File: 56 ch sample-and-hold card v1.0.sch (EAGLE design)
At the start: 140 parts, among them IC1 74HCT4051D, IC10 TL074JT, IC11 74HCT4051D, IC12 TL074JT, IC13 TL074JT, IC14 74HCT4051D, IC15 TL074JT, IC16 TL074JT, IC17 74HCT4051D, IC18 TL074JT, IC19 TL074JT, IC2 DAC8586D, IC20 74HCT4051D, IC21 TL074JT, IC22 TL074JT, IC26 74HCT4051D, IC27 TL074JT, IC28 TL074JT, IC3 TL074JT, IC5 78L05F, IC6 TL074JT, IC7 74HCT4051D, IC8 TL074JT, IC9 TL074JT, X2 FEMALE, X3 FEMALE, X4 DNM, X5 DNM, X7 FEMALE, X8 FEMALE, X9 DNM

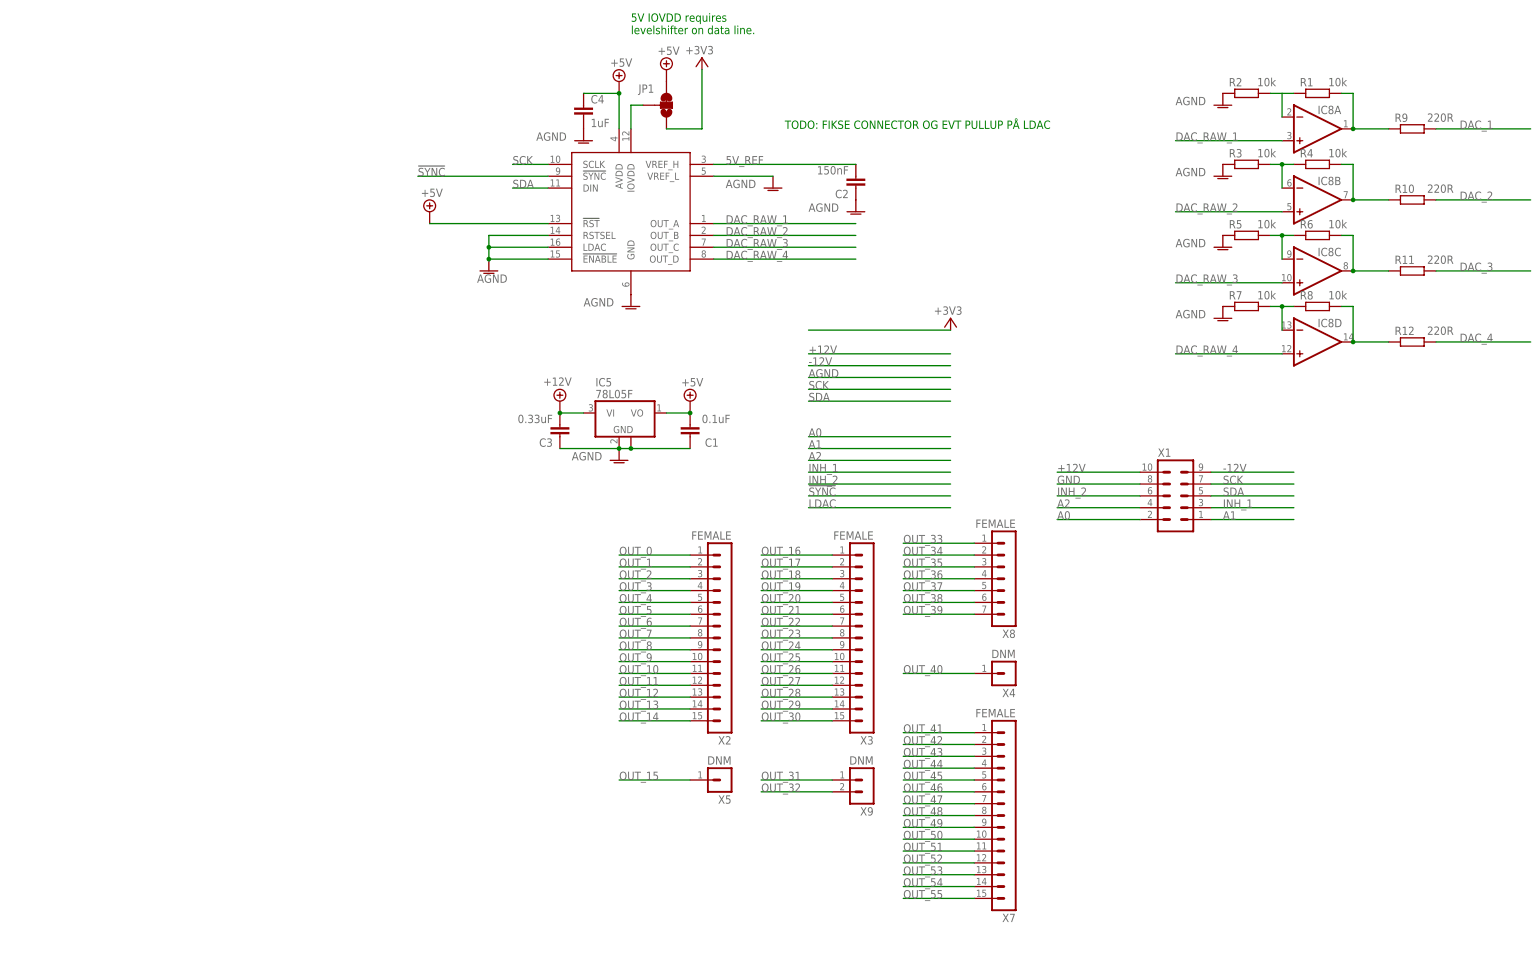
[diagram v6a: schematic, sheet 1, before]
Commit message: Fixed ground bug, finished tracing
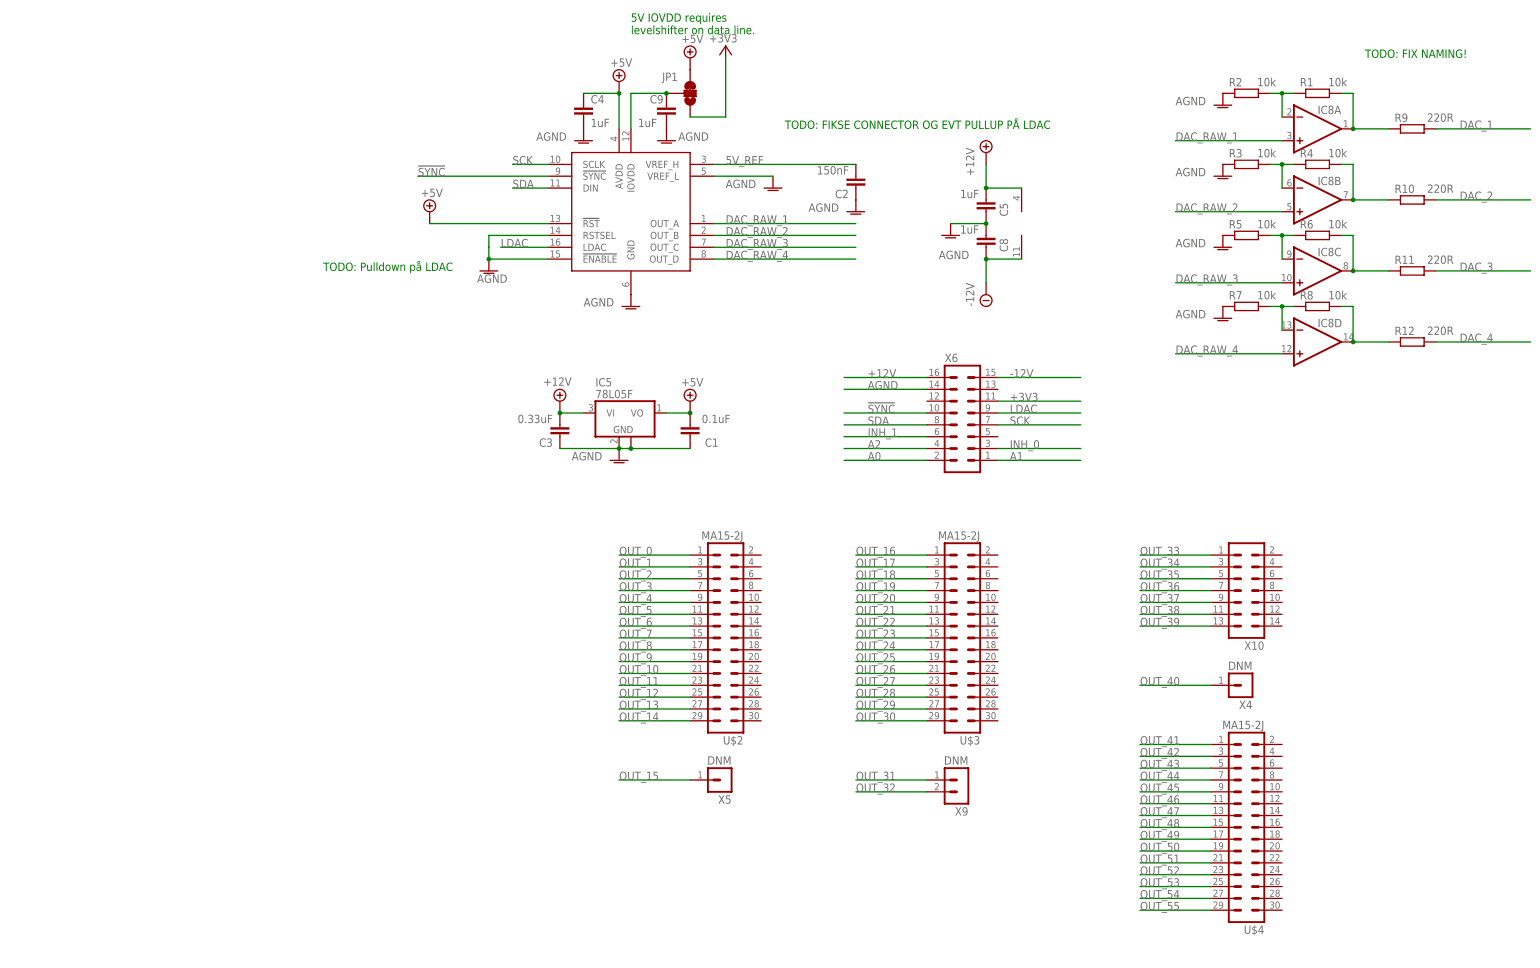
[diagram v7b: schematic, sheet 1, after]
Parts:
- removed X1: (no value), joakim:MA05-2J
- removed X2, X3, X7: FEMALE, joakim:MA15-1JC
- removed X8: FEMALE, joakim:MA07-1JC
- added C5, C8, C9: 1uF, joakim:C-EU-J0402
- added U$2, U$3, U$4: MA15-2J, joakim:MA15-2J
- added X10: (no value), joakim:MA07-2J
- added X6: (no value), joakim:MA08-2J
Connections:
- removed net GND: X1.8
- removed net INH_2: IC11A.INH, IC14A.INH, IC17A.INH, X1.6
- removed net N$6: R1.1, R2.2
- new net INH_0: IC1A.INH, IC20A.INH, IC26A.INH, IC7A.INH, X6.3
- new net LDAC: IC2.LDAC, X6.9
- net !SYNC: now also X6.10
- net +12V: now also C5.1, IC8P.V+, X6.16; no longer X1.10
- net +3V3: now also X6.11
- net -12V: now also C8.2, IC8P.V-, X6.15; no longer X1.9
- net A0: now also X6.2; no longer X1.2
- net A1: now also X6.1; no longer X1.1
- net A2: now also X6.4; no longer X1.4
- net AGND: now also C5.2, C8.1, C9.2, X6.14; no longer IC2.LDAC
- net INH_1: now also IC11A.INH, IC14A.INH, IC17A.INH, X6.6; no longer IC1A.INH, IC20A.INH, IC26A.INH, IC7A.INH, X1.3
- net N$1: now also C9.1
- net N$2: now also R1.1, R2.2
- net OUT_0: now also U$2.1; no longer X2.1
- net OUT_1: now also U$2.3; no longer X2.2
- net OUT_10: now also U$2.21; no longer X2.11
- net OUT_11: now also U$2.23; no longer X2.12
- net OUT_12: now also U$2.25; no longer X2.13
- net OUT_13: now also U$2.27; no longer X2.14
- net OUT_14: now also U$2.29; no longer X2.15
- net OUT_16: now also U$3.1; no longer X3.1
- net OUT_17: now also U$3.3; no longer X3.2
- net OUT_18: now also U$3.5; no longer X3.3
- net OUT_19: now also U$3.7; no longer X3.4
- net OUT_2: now also U$2.5; no longer X2.3
- net OUT_20: now also U$3.9; no longer X3.5
- net OUT_21: now also U$3.11; no longer X3.6
- net OUT_22: now also U$3.13; no longer X3.7
- net OUT_23: now also U$3.15; no longer X3.8
- net OUT_24: now also U$3.17; no longer X3.9
- net OUT_25: now also U$3.19; no longer X3.10
- net OUT_26: now also U$3.21; no longer X3.11
- net OUT_27: now also U$3.23; no longer X3.12
- net OUT_28: now also U$3.25; no longer X3.13
- net OUT_29: now also U$3.27; no longer X3.14
- net OUT_3: now also U$2.7; no longer X2.4
- net OUT_30: now also U$3.29; no longer X3.15
- net OUT_33: now also X10.1; no longer X8.1
- net OUT_34: now also X10.3; no longer X8.2
- net OUT_35: now also X10.5; no longer X8.3
- net OUT_36: now also X10.7; no longer X8.4
- net OUT_37: now also X10.9; no longer X8.5
- net OUT_38: now also X10.11; no longer X8.6
- net OUT_39: now also X10.13; no longer X8.7
- net OUT_4: now also U$2.9; no longer X2.5
- net OUT_41: now also U$4.1; no longer X7.1
- net OUT_42: now also U$4.3; no longer X7.2
- net OUT_43: now also U$4.5; no longer X7.3
- net OUT_44: now also U$4.7; no longer X7.4
- net OUT_45: now also U$4.9; no longer X7.5
- net OUT_46: now also U$4.11; no longer X7.6
- net OUT_47: now also U$4.13; no longer X7.7
- net OUT_48: now also U$4.15; no longer X7.8
- net OUT_49: now also U$4.17; no longer X7.9
- net OUT_5: now also U$2.11; no longer X2.6
- net OUT_50: now also U$4.19; no longer X7.10
- net OUT_51: now also U$4.21; no longer X7.11
- net OUT_52: now also U$4.23; no longer X7.12
- net OUT_53: now also U$4.25; no longer X7.13
- net OUT_54: now also U$4.27; no longer X7.14
- net OUT_55: now also U$4.29; no longer X7.15
- net OUT_6: now also U$2.13; no longer X2.7
- net OUT_7: now also U$2.15; no longer X2.8
- net OUT_8: now also U$2.17; no longer X2.9
- net OUT_9: now also U$2.19; no longer X2.10
- net SCK: now also X6.7; no longer X1.7
- net SDA: now also X6.8; no longer X1.5
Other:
- note added: "TODO: FIX NAMING!"
- note added: "TODO: Pulldown på LDAC"
- moved on the sheet: JP1, X4, X9

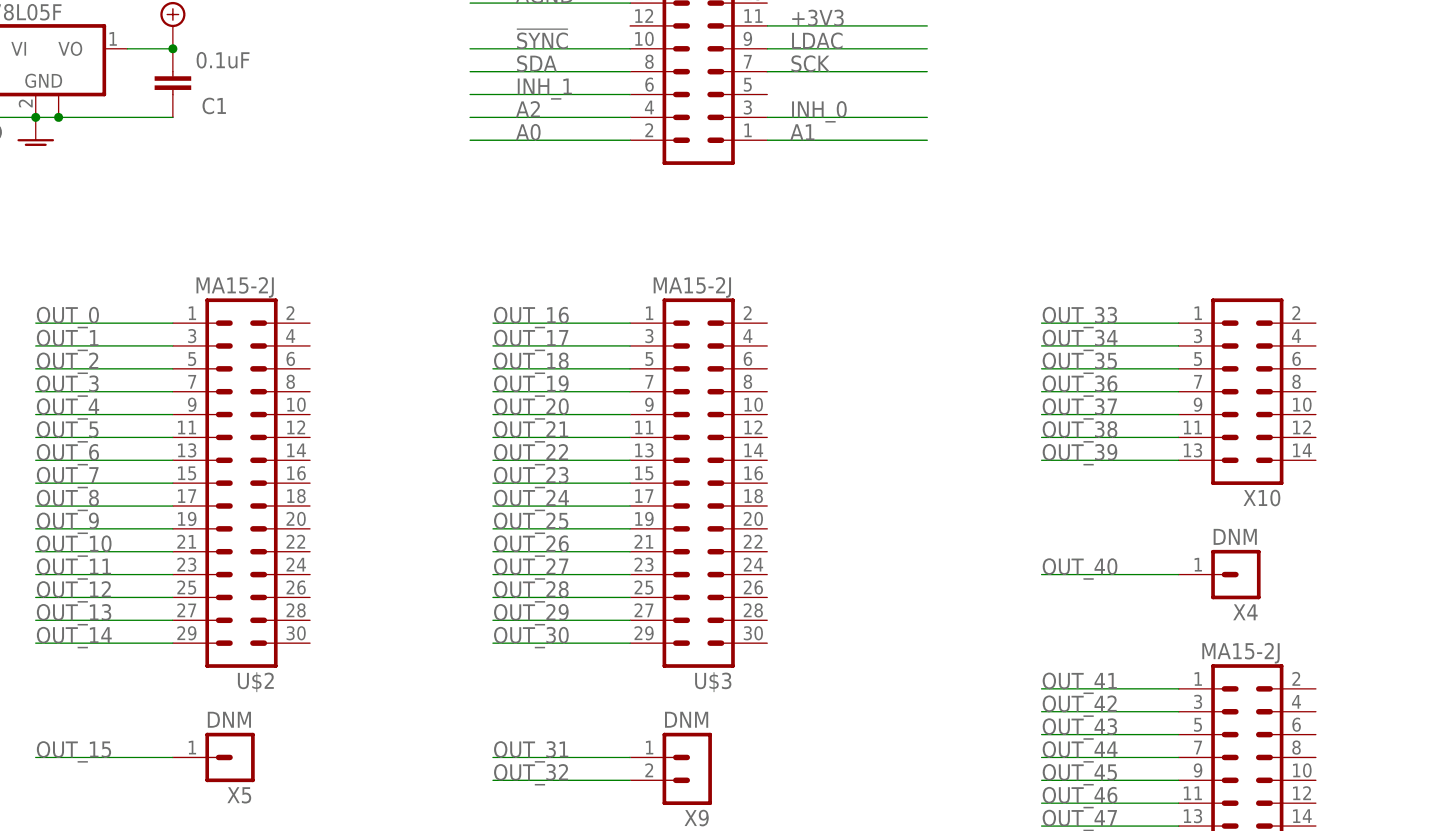
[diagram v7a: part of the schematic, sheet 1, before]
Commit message: Changed dac footprint
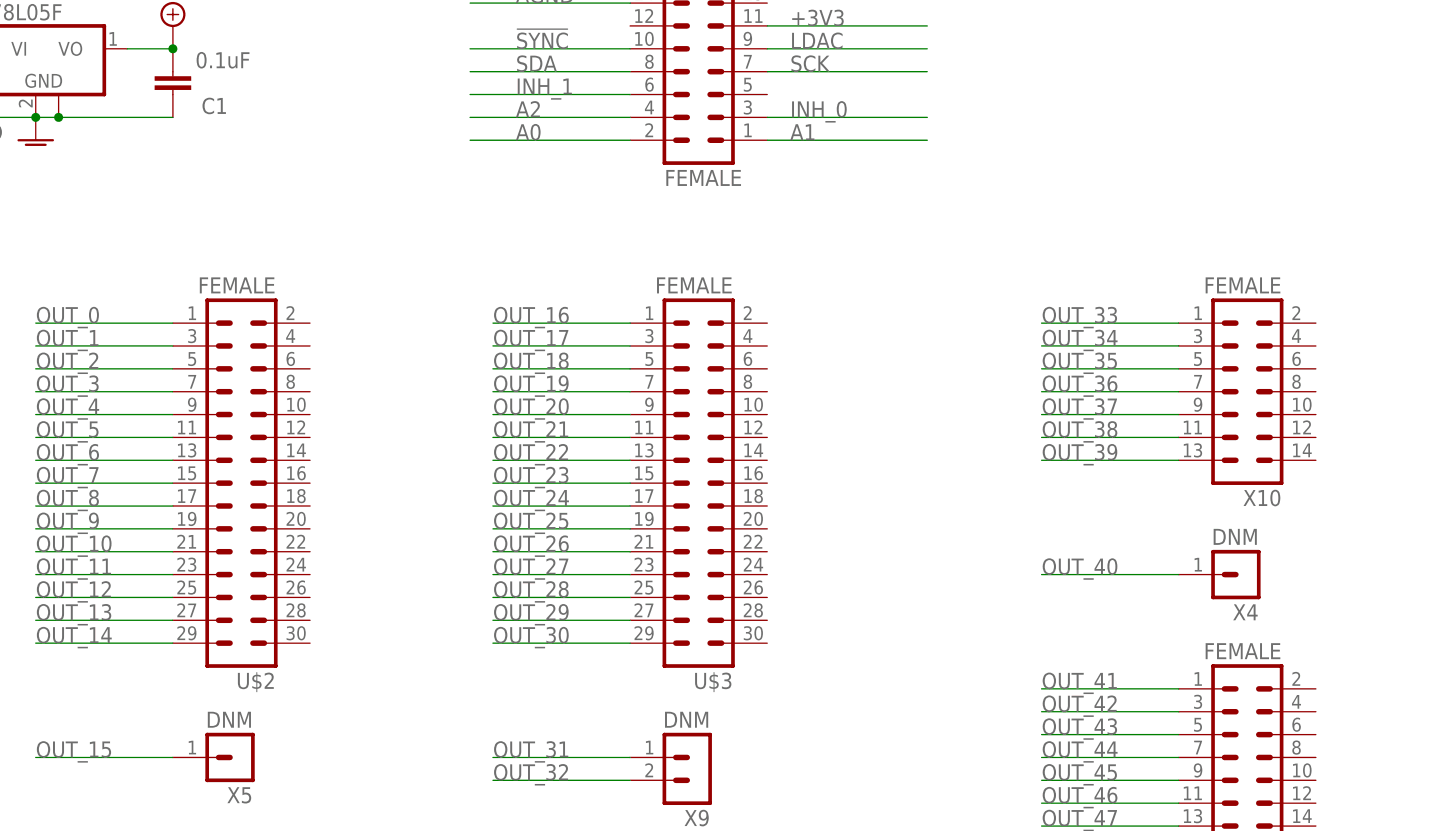
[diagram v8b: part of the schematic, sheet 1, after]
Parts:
- IC2: value DAC8586D -> DAC8586F; device joakim:DAC8586D -> joakim:DAC8586F
- U$2, U$3, U$4: value MA15-2J -> FEMALE
- X10, X6: value (none) -> FEMALE
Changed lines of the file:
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@@
 <part name="C119" library="joakim" deviceset="C-EU-J" device="0402" value="1uF"/>
 <part name="AGND101" library="supply1" deviceset="AGND" device=""/>
-<part name="IC2" library="joakim" deviceset="DAC8586" device="D"/>
+<part name="IC2" library="joakim" deviceset="DAC8586" device="F" value="DAC8586F"/>
 <part name="AGND1" library="supply1" deviceset="AGND" device=""/>
 <part name="AGND6" library="supply1" deviceset="AGND" device=""/>
@@
 <part name="R11" library="rcl" library_urn="urn:adsk.eagle:library:334" deviceset="R-EU_" device="R0603" package3d_urn="urn:adsk.eagle:package:23555/3" value="220R"/>
 <part name="R12" library="rcl" library_urn="urn:adsk.eagle:library:334" deviceset="R-EU_" device="R0603" package3d_urn="urn:adsk.eagle:package:23555/3" value="220R"/>
-<part name="X6" library="joakim" deviceset="MA08-2J" device=""/>
-<part name="X10" library="joakim" deviceset="MA07-2J" device=""/>
-<part name="U$2" library="joakim" deviceset="MA15-2J" device=""/>
-<part name="U$3" library="joakim" deviceset="MA15-2J" device=""/>
-<part name="U$4" library="joakim" deviceset="MA15-2J" device=""/>
+<part name="X6" library="joakim" deviceset="MA08-2J" device="" value="FEMALE"/>
+<part name="X10" library="joakim" deviceset="MA07-2J" device="" value="FEMALE"/>
+<part name="U$2" library="joakim" deviceset="MA15-2J" device="" value="FEMALE"/>
+<part name="U$3" library="joakim" deviceset="MA15-2J" device="" value="FEMALE"/>
+<part name="U$4" library="joakim" deviceset="MA15-2J" device="" value="FEMALE"/>
 <part name="C5" library="joakim" deviceset="C-EU-J" device="0402" value="1uF"/>
 <part name="P+1" library="supply2" library_urn="urn:adsk.eagle:library:372" deviceset="+12V" device=""/>
